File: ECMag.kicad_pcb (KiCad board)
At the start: 2 copper layers, 113 x 59.7 mm, 48 parts, among them J1 Conn_01x12, J2 Conn_01x05, J3 Conn_01x04, J4 USB_B, J5 Barrel_Jack_SW, J6 Conn_01x04, K1 Switch, K2 Switch, K3 Switch, K4 Switch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

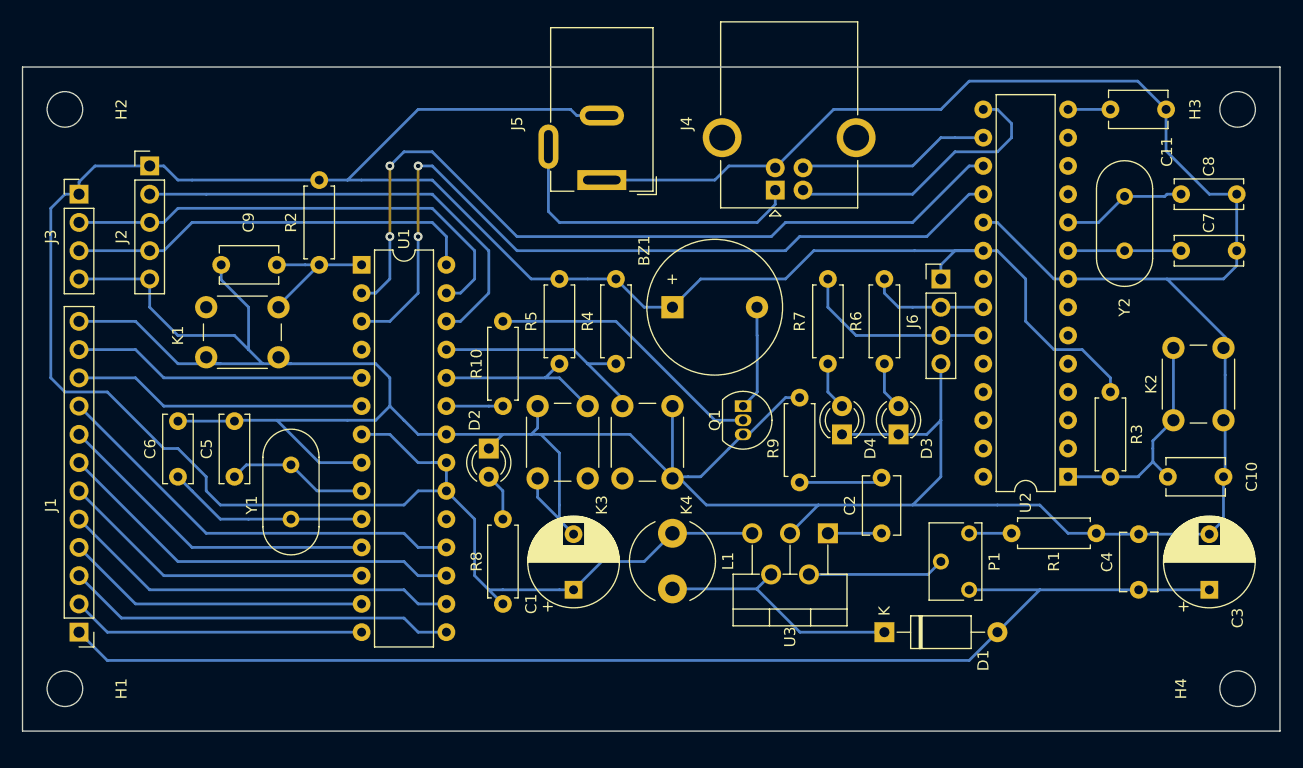
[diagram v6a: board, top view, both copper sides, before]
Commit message: Paso de los tracks de 0.25 a 0.45, tracks de senhales y potencia
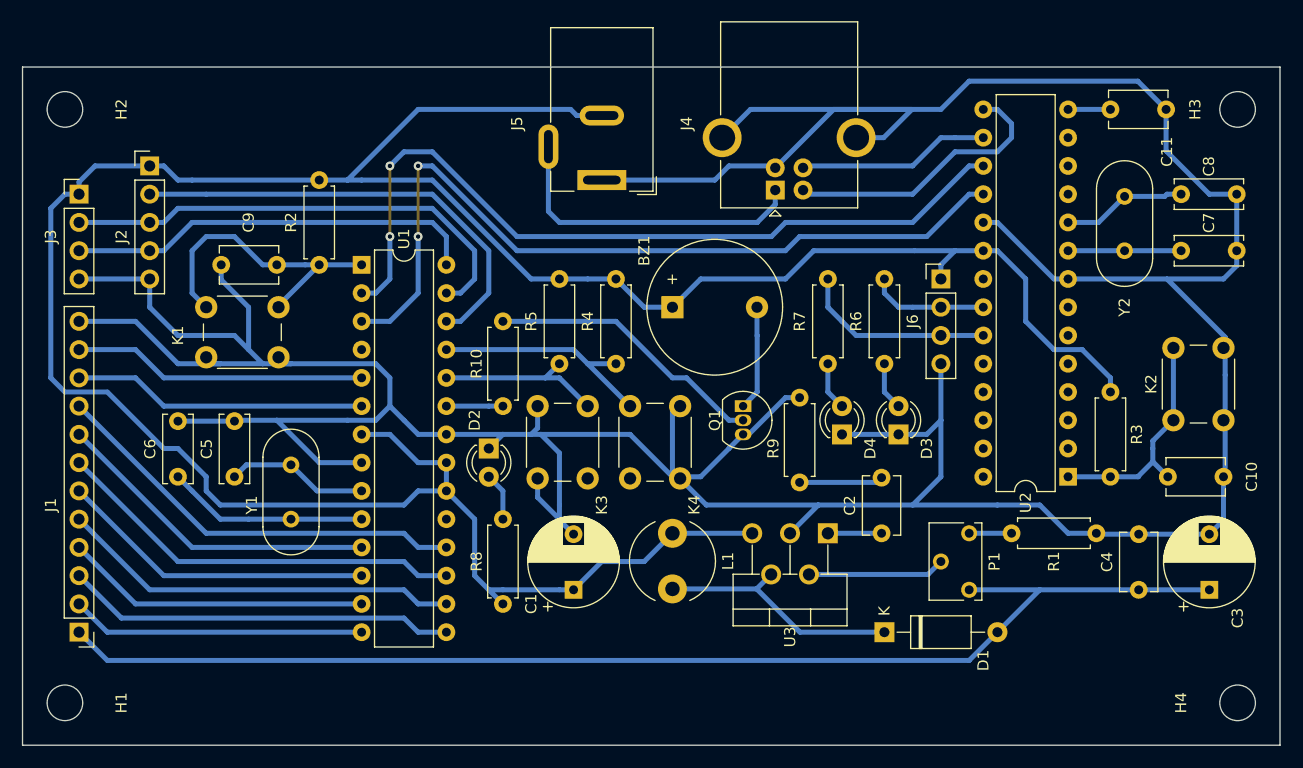
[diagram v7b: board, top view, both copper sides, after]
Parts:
- moved H1 1.27 mm to (87.6, 106.7)
- moved H4 1.27 mm to (193.0, 106.7)
- moved K4 0.69 mm to (138.4, 86.5)
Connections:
- J4 pad 5: Net-(J4-Pad5) -> GND
- U1 pad 19: (no net) -> Net-(U1-Pad19)
- U1 pad 4: (no net) -> Net-(U1-Pad4)
- U2 pad 11: (no net) -> Net-(U2-Pad11)
- U2 pad 12: (no net) -> Net-(U2-Pad12)
- U2 pad 13: (no net) -> Net-(U2-Pad13)
- U2 pad 2: (no net) -> Net-(U2-Pad2)
- U2 pad 21: (no net) -> Net-(U2-Pad21)
- U2 pad 24: (no net) -> Net-(U2-Pad24)
- U2 pad 25: (no net) -> Net-(U2-Pad25)
- U2 pad 26: (no net) -> Net-(U2-Pad26)
- U2 pad 27: (no net) -> Net-(U2-Pad27)
- U2 pad 28: (no net) -> Net-(U2-Pad28)
- U2 pad 3: (no net) -> Net-(U2-Pad3)
- U2 pad 4: (no net) -> Net-(U2-Pad4)
- U2 pad 5: (no net) -> Net-(U2-Pad5)
- U2 pad 6: (no net) -> Net-(U2-Pad6)
- U2 pad 7: (no net) -> Net-(U2-Pad7)
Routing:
- net GND: track 363.1 -> 387.3 mm
- net Net-(C9-Pad1): track 13.0 -> 27.8 mm
- net /Btn_NL: track 20.7 -> 21.4 mm
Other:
- board size 113 x 59.7 mm -> 113 x 61 mm
- net class Default: trace_width 0.25 -> 0.45
- net class Potencia added: clearance 0.2, trace_width 1, via_dia 0.8, via_drill 0.4
- net class Senhal added: clearance 0.2, trace_width 0.45, via_dia 0.8, via_drill 0.4

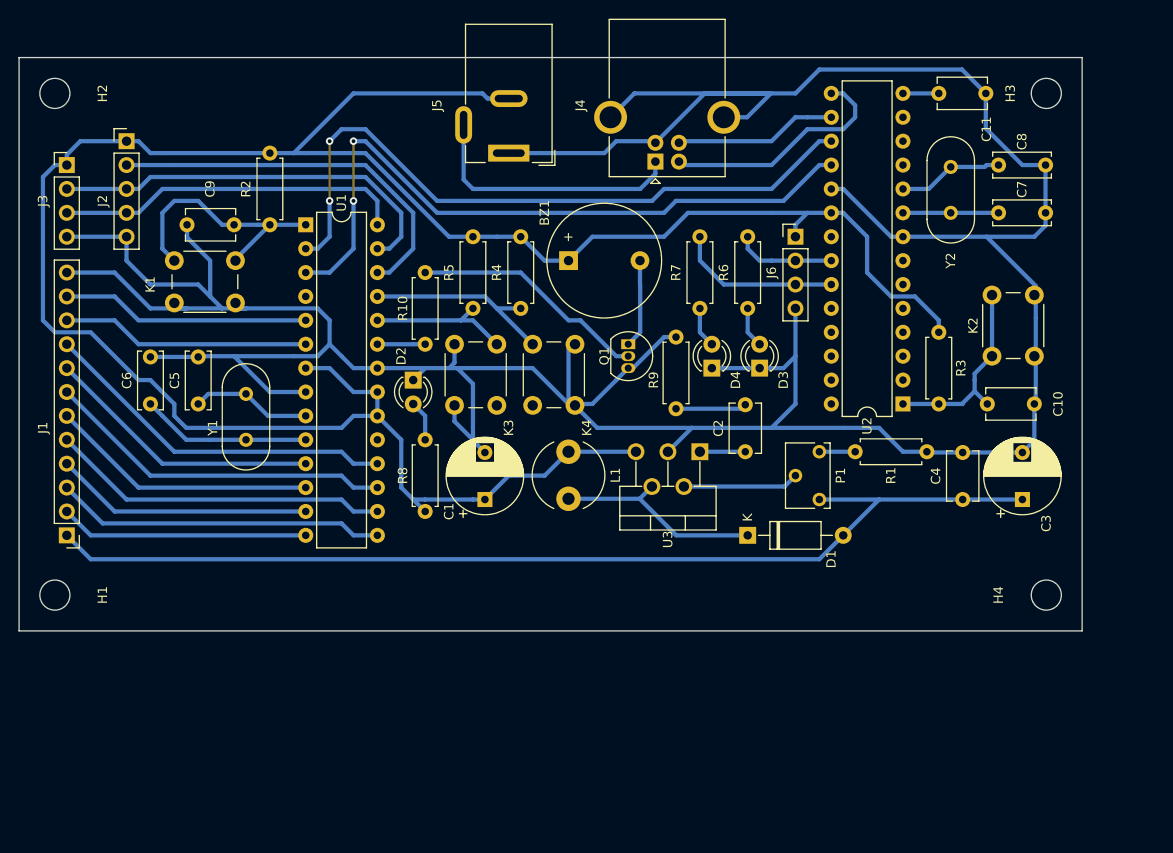
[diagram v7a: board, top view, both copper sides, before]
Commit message: Planos de Tierra de Fuente Switchin de 12V y Plano General
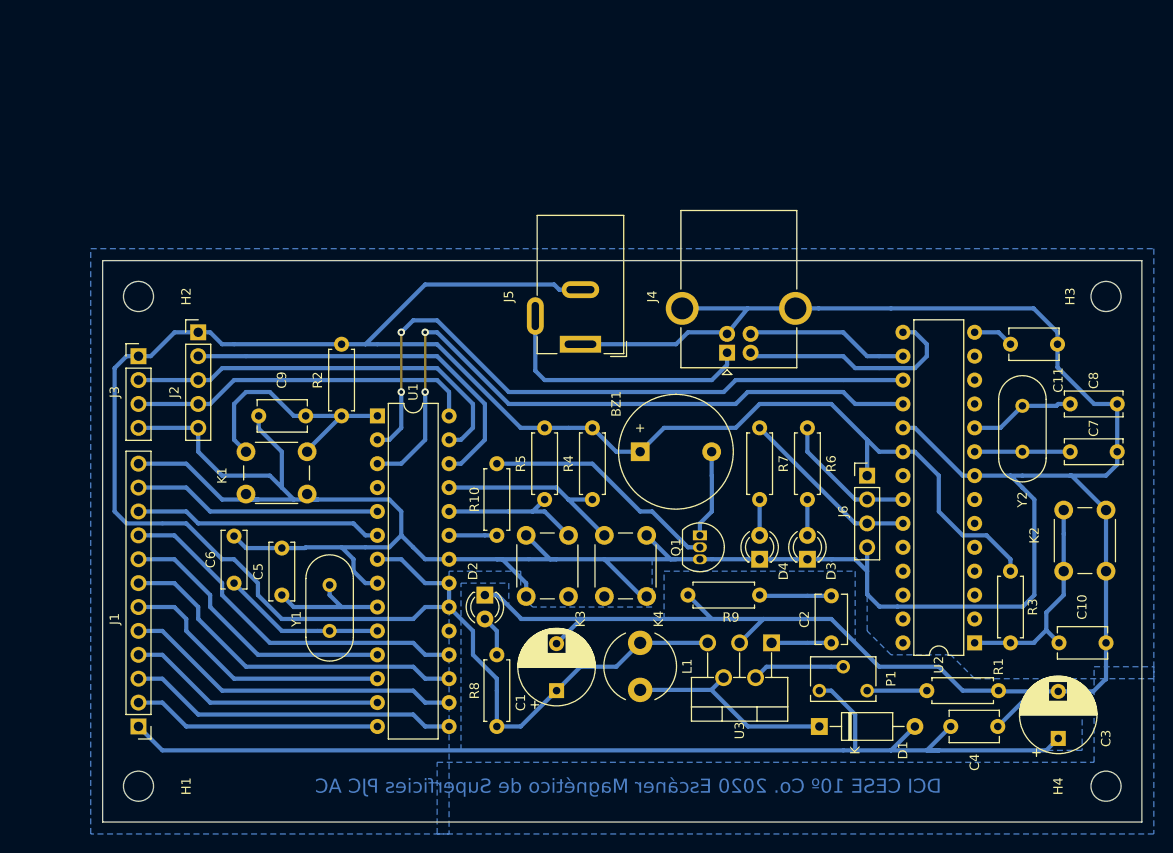
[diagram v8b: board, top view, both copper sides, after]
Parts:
- J1: value Conn_01x12 -> Cn_01x12
- J2: value Conn_01x05 -> Cn_01x05
- J3, J6: value Conn_01x04 -> Cn_01x04
- moved C11 27.7 mm to (189.2, 80.0)
- moved J6 26.5 mm to (174.0, 94.0)
- moved R1 26.5 mm to (180.3, 116.8)
- moved C10 26.5 mm to (194.4, 111.8)
- moved C8 26.5 mm to (195.6, 86.4)
- moved R3 26.5 mm to (189.2, 104.1)
- moved U2 26.5 mm to (185.4, 111.8)
- moved C7 26.5 mm to (195.6, 91.4)
- moved Y2 26.5 mm to (190.5, 91.4)
- moved C3 25.7 mm to (194.3, 121.9)
- moved C4 24.2 mm to (182.9, 120.7), turned to 0 degrees
- moved D2 24.1 mm to (133.3, 106.7)
- moved R8 24.1 mm to (134.6, 120.7)
- moved K2 24.1 mm to (194.9, 104.1)
- moved H2 23.3 mm to (96.5, 74.9)
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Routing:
- net GND: track 387.3 -> 414.9 mm
- net +12V: track 111.6 -> 116.5 mm
- net /TxSgn: track 10.7 -> 14.8 mm
- net Net-(P1-Pad2): track 12.3 -> 9.80 mm
- net Net-(C10-Pad1): track 21.2 -> 23.7 mm
- net Net-(P1-Pad3): track 3.81 -> 6.35 mm
- net +5V: track 251.7 -> 254.2 mm
- net /RxTx: track 72.9 -> 70.8 mm
- net /RxSgn: track 17.6 -> 19.4 mm
- net Net-(C2-Pad1): track 5.08 -> 6.35 mm
- net /TxRx: track 73.6 -> 72.6 mm
- net /D-: track 25.3 -> 24.3 mm
- net /a8: track 38.3 -> 39.0 mm
- net /a7: track 29.6 -> 30.4 mm
- net Net-(C6-Pad1): track 18.1 -> 17.3 mm
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- added copper zone on B.Cu, net GND
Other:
- board size 113 x 61 mm -> 110.5 x 59.7 mm
- net class Potencia: trace_width 1 -> 0.45
- board text added: "DCI CESE 10º Co. 2020 Escáner Magnético de Superficies PJC AC"
